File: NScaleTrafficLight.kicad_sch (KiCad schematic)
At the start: 10 parts, among them J1 Conn_01x01_Pin, J2 Conn_01x01_Pin, J3 Conn_01x01_Pin, J4 Conn_01x01_Pin

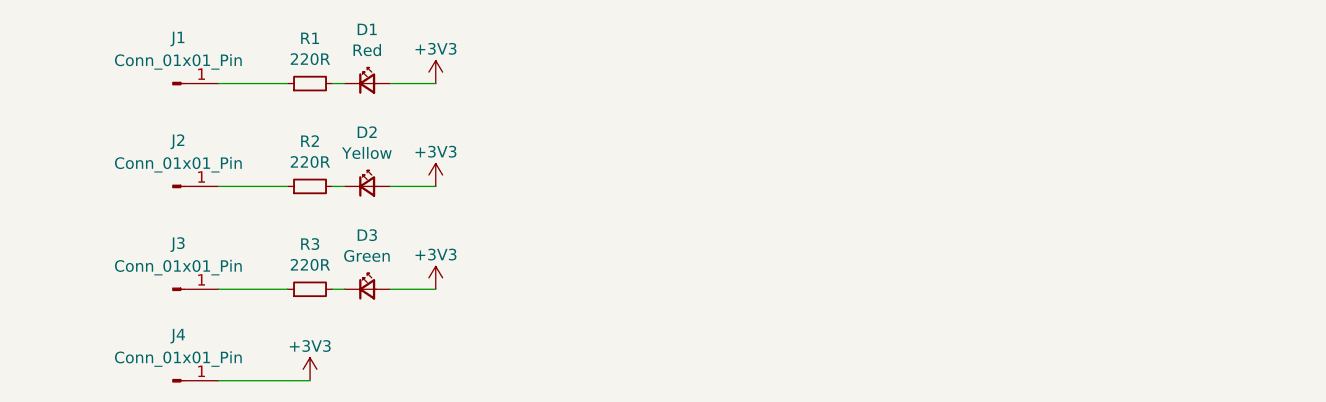
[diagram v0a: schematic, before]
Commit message: Add resistor network, 4th signal light option
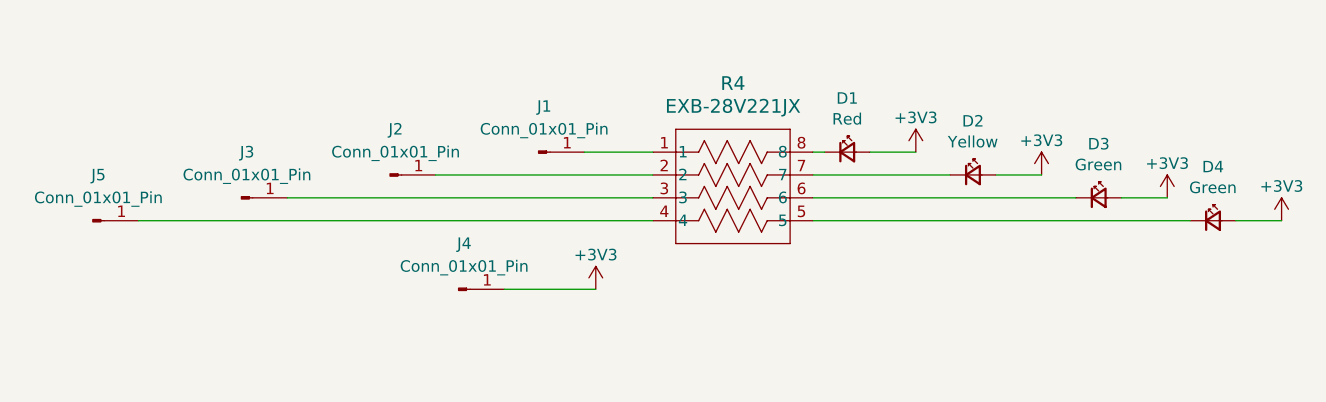
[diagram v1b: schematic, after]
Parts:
- removed R1, R2, R3: 220R, Resistor_SMD:R_0402_1005Metric_Pad0.72x0.64mm_HandSolder, symbol Device:R_Small
- added D4: Green, LED_SMD:LED_0402_1005Metric, symbol Device:LED_Small
- added J5: Conn_01x01_Pin, Connector_Wire:SolderWirePad_1x01_SMD_1x2mm, symbol Connector:Conn_01x01_Pin
- added R4: EXB-28V221JX, footprints:EXB28V_PAN, symbol ResistorNetwork:EXB-28V221JX
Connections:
- net +3V3: now also D4.2 (A)
- net at J1.1 (Pin_1): now also R4.1
- net at D1.1 (K): now also R4.8
- net at J3.1 (Pin_1): now also R4.3
- net at D3.1 (K): now also R4.6
- net at J2.1 (Pin_1): now also R4.2
- net at D2.1 (K): now also R4.7
- new net: D4.1 (K), R4.5
- new net: J5.1 (Pin_1), R4.4
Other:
- moved on the sheet: D1, D2, D3, J1, J2, J3, J4
